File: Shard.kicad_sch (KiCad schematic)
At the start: 5 parts, among them J1 USB_C_Receptacle_USB2.0_16P, U1 ESP32-S3

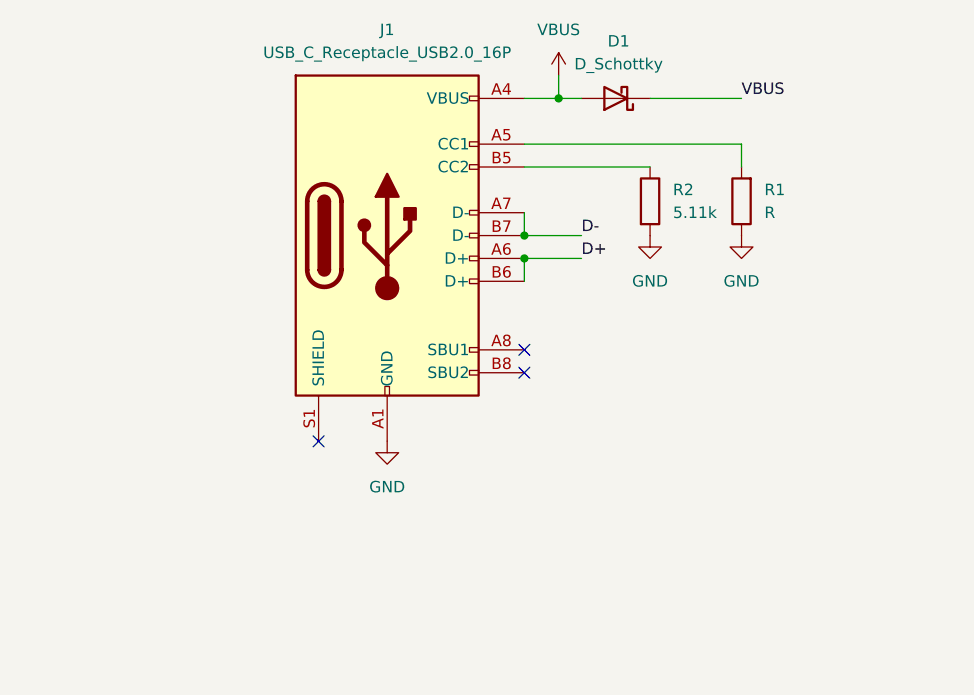
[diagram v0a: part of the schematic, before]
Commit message: USB-C Wiring
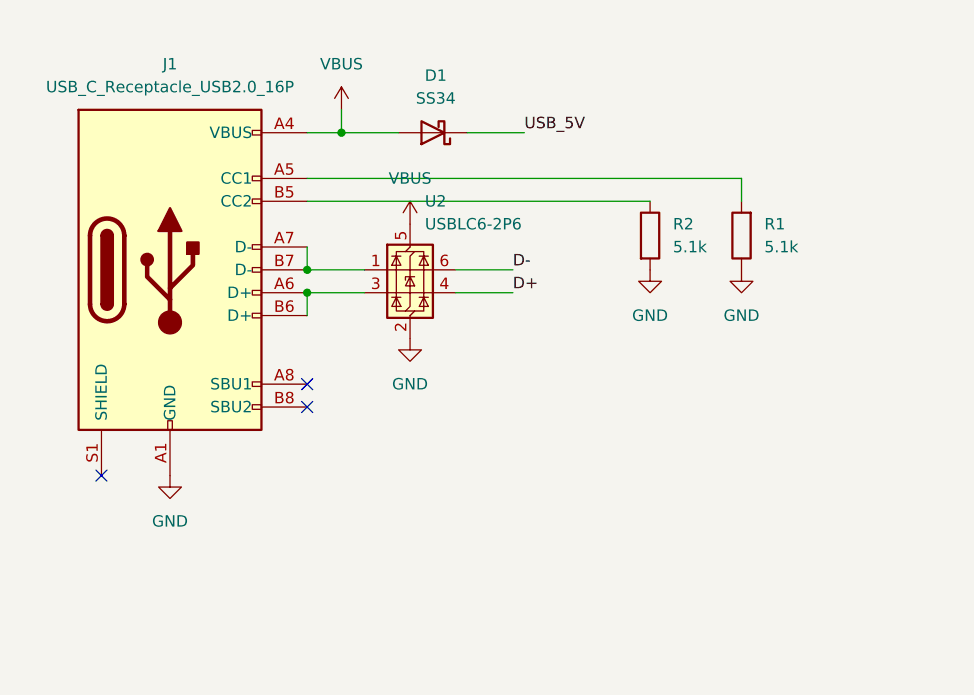
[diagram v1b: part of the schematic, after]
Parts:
- added U2: USBLC6-2P6, Package_TO_SOT_SMD:SOT-666, symbol Power_Protection:USBLC6-2P6
- D1: value D_Schottky -> SS34; footprint (none) -> Diode_SMD:D_SMA; REF (none) -> C8678
- J1: footprint (none) -> Connector_USB:USB_C_Receptacle_GCT_USB4105-xx-A_16P_TopMnt_Horizontal; REF (none) -> C2927038
- R1: value R -> 5.1k; footprint (none) -> Resistor_SMD:R_0402_1005Metric; REF (none) -> C294638
- R2: value 5.11k -> 5.1k; footprint (none) -> Resistor_SMD:R_0402_1005Metric; REF (none) -> C294638
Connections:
- net D+: now also U2.4 (I/O2); no longer J1.A6 (D+), J1.B6 (D+)
- net D-: now also U2.6 (I/O1); no longer J1.A7 (D-), J1.B7 (D-)
- net GND: now also U2.2 (GND)
- net VBUS: now also U2.5 (VBUS); no longer D1.1 (K)
- new net: J1.A6 (D+), J1.B6 (D+), U2.3 (I/O2)
- new net: J1.A7 (D-), J1.B7 (D-), U2.1 (I/O1)
- new net USB_5V: D1.1 (K)
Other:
- moved on the sheet: D1, J1, R1, R2

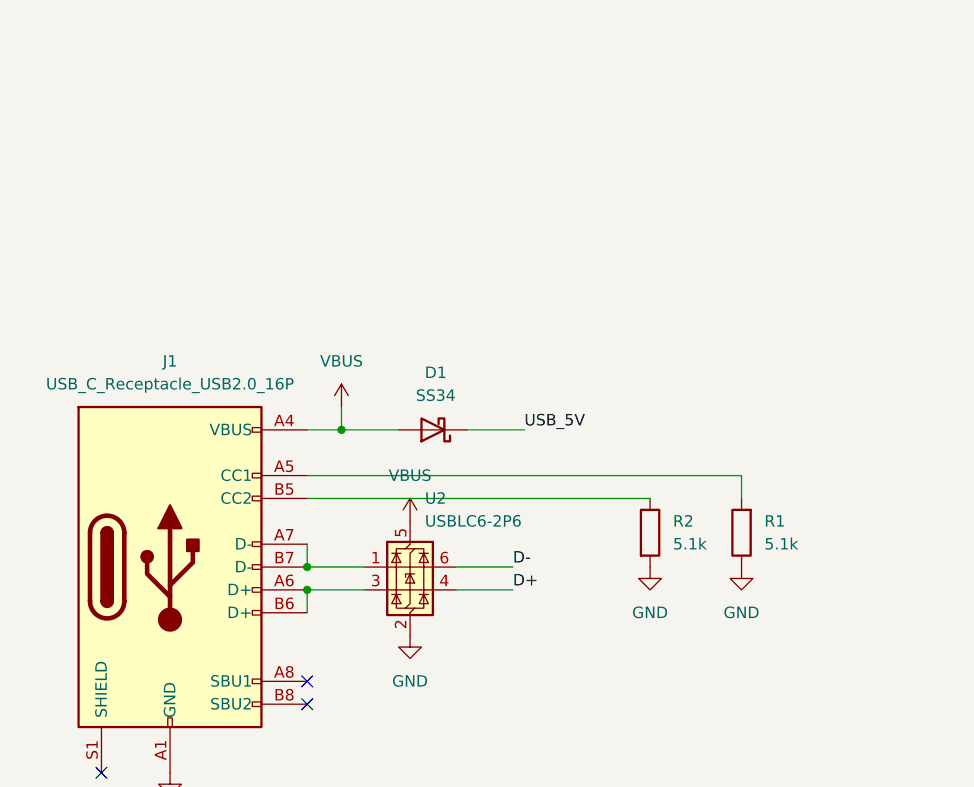
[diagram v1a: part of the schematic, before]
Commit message: Add voltage regulator
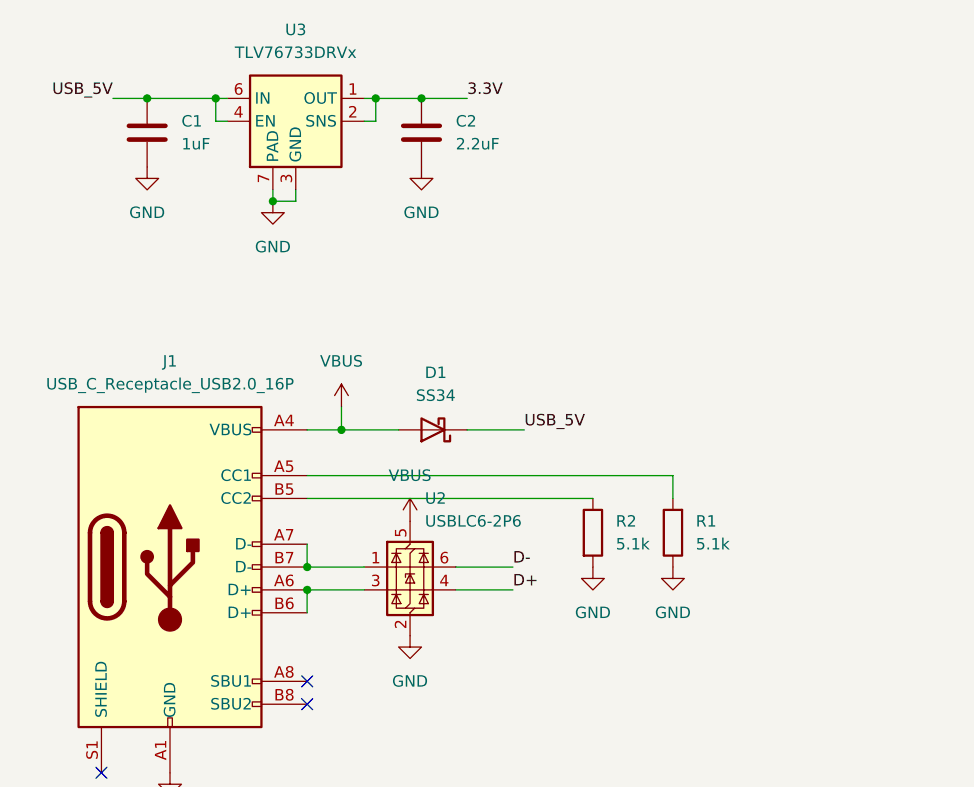
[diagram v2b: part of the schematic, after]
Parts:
- added C1: 1uF, Capacitor_SMD:C_0603_1608Metric, symbol Device:C
- added C2: 2.2uF, Capacitor_SMD:C_0402_1005Metric, symbol Device:C
- added U3: TLV76733DRVx, Package_SON:WSON-6-1EP_2x2mm_P0.65mm_EP1x1.6mm_ThermalVias, symbol Regulator_Linear:TLV76733DRVx
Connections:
- net GND: now also C1.2, C2.2, U3.3 (GND), U3.5 (GND), U3.7 (PAD)
- net USB_5V: now also C1.1, U3.4 (EN), U3.6 (IN)
- new net 3.3V: C2.1, U3.1 (OUT), U3.2 (SNS)
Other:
- moved on the sheet: R1, R2

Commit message: Add battery connector
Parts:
- added D2: SS34, Diode_SMD:D_SMA, symbol Device:D_Schottky
- added J2: Conn_01x02_Pin, symbol Connector:Conn_01x02_Pin
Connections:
- net GND: now also J2.2 (Pin_2)
- net USB_5V renamed V_BAT
- net V_BAT: now also D2.1 (K)
- new net: D2.2 (A), J2.1 (Pin_1)

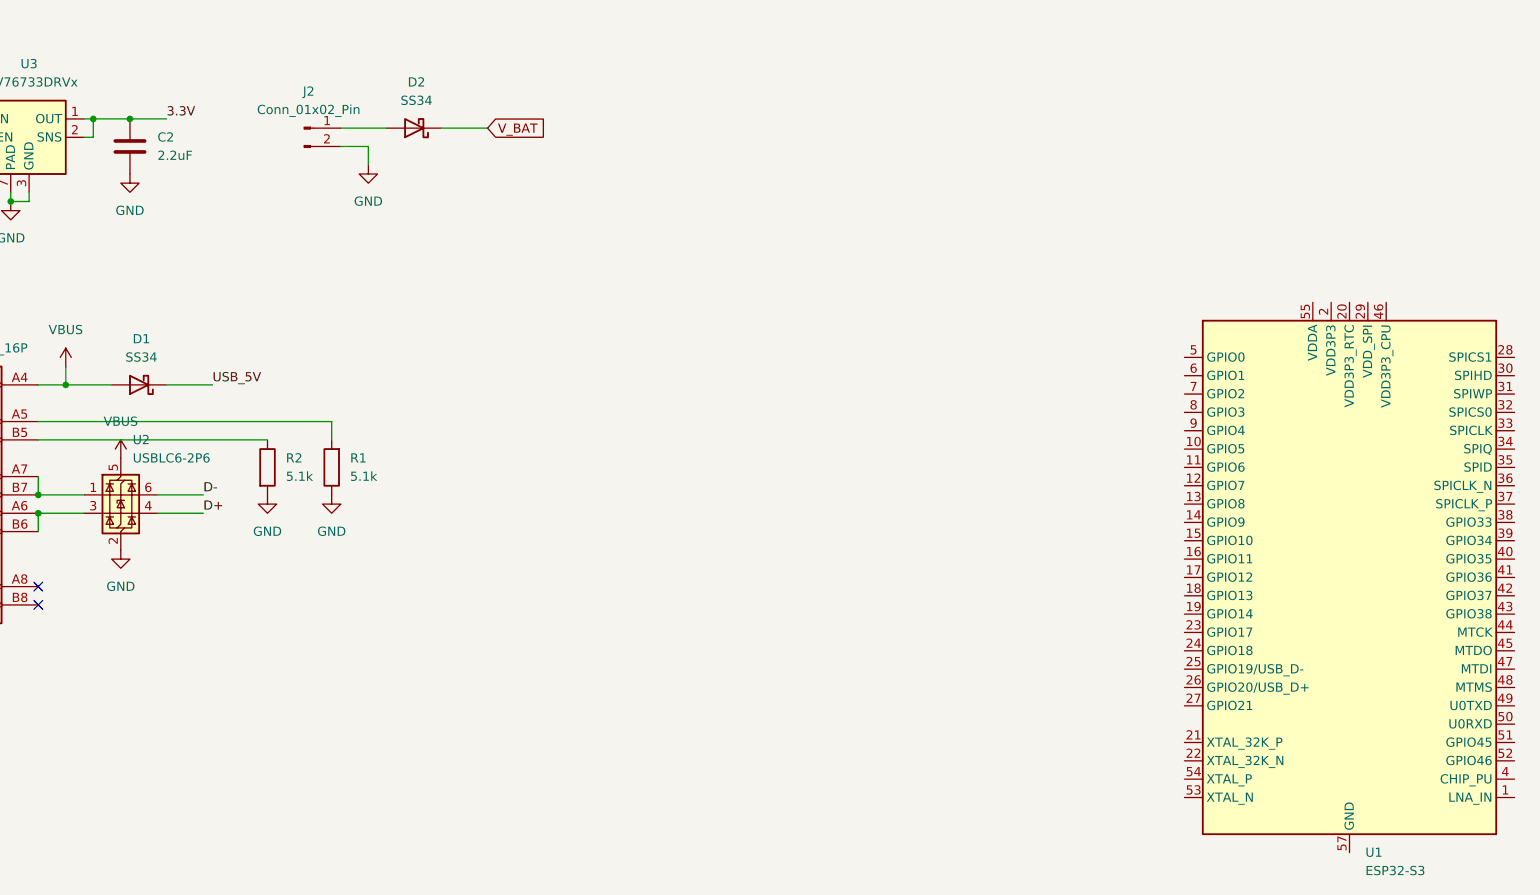
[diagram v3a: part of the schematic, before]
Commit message: Add missing footprint and parts
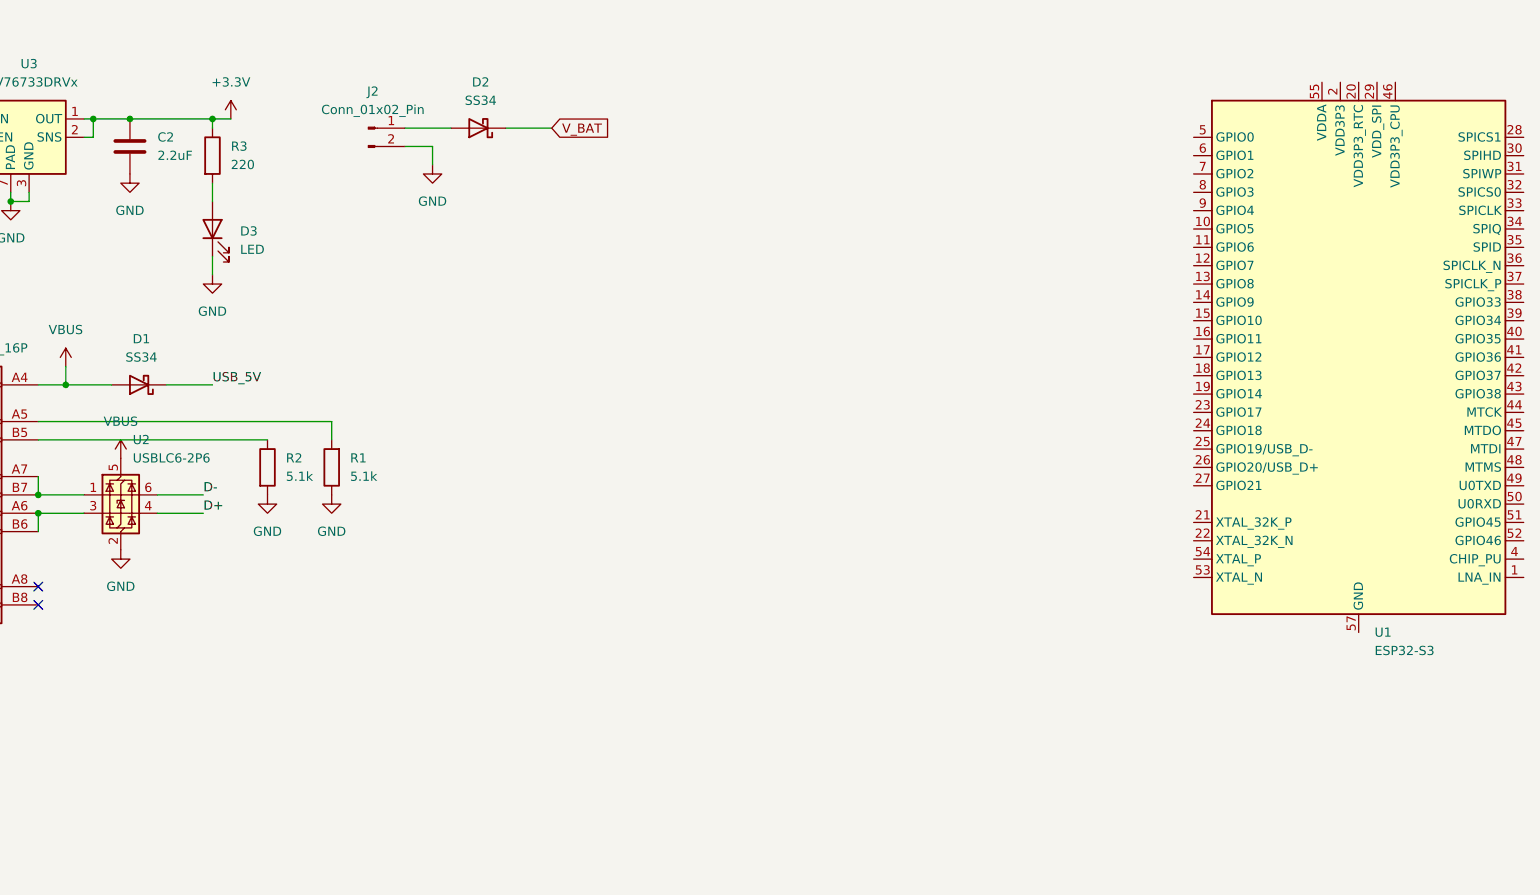
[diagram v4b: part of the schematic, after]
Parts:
- added D3: LED, LED_SMD:LED_0805_2012Metric, symbol Device:LED
- added R3: 220, Resistor_SMD:R_0805_2012Metric, symbol Device:R
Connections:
- net GND: now also D3.1 (K)
- net 3.3V renamed +3.3V
- net +3.3V: now also R3.1
- new net: D3.2 (A), R3.2
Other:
- moved on the sheet: D2, J2, U1

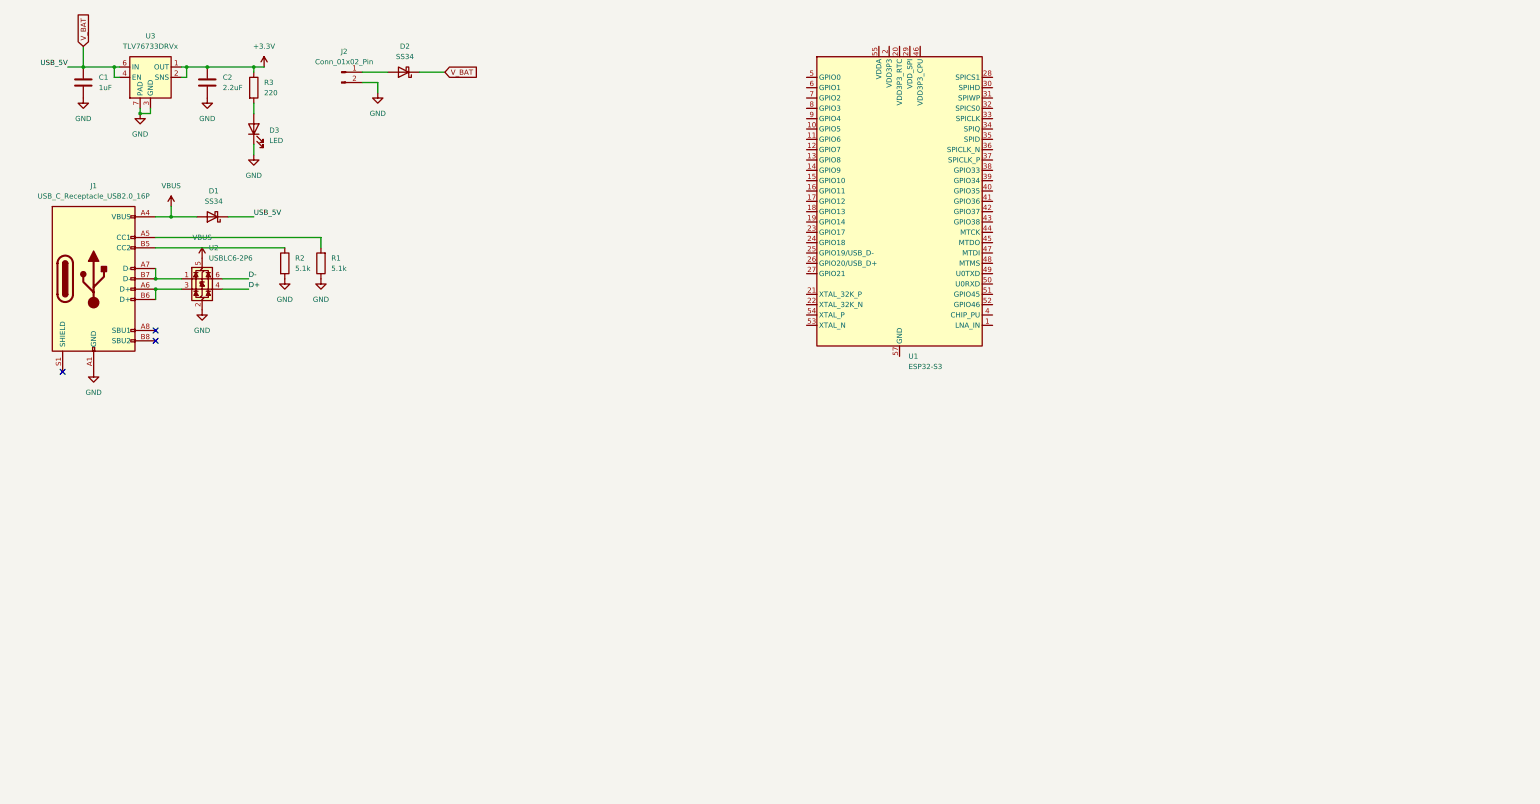
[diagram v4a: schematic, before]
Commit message: Add MCU power schematic + Footprint and part assignation
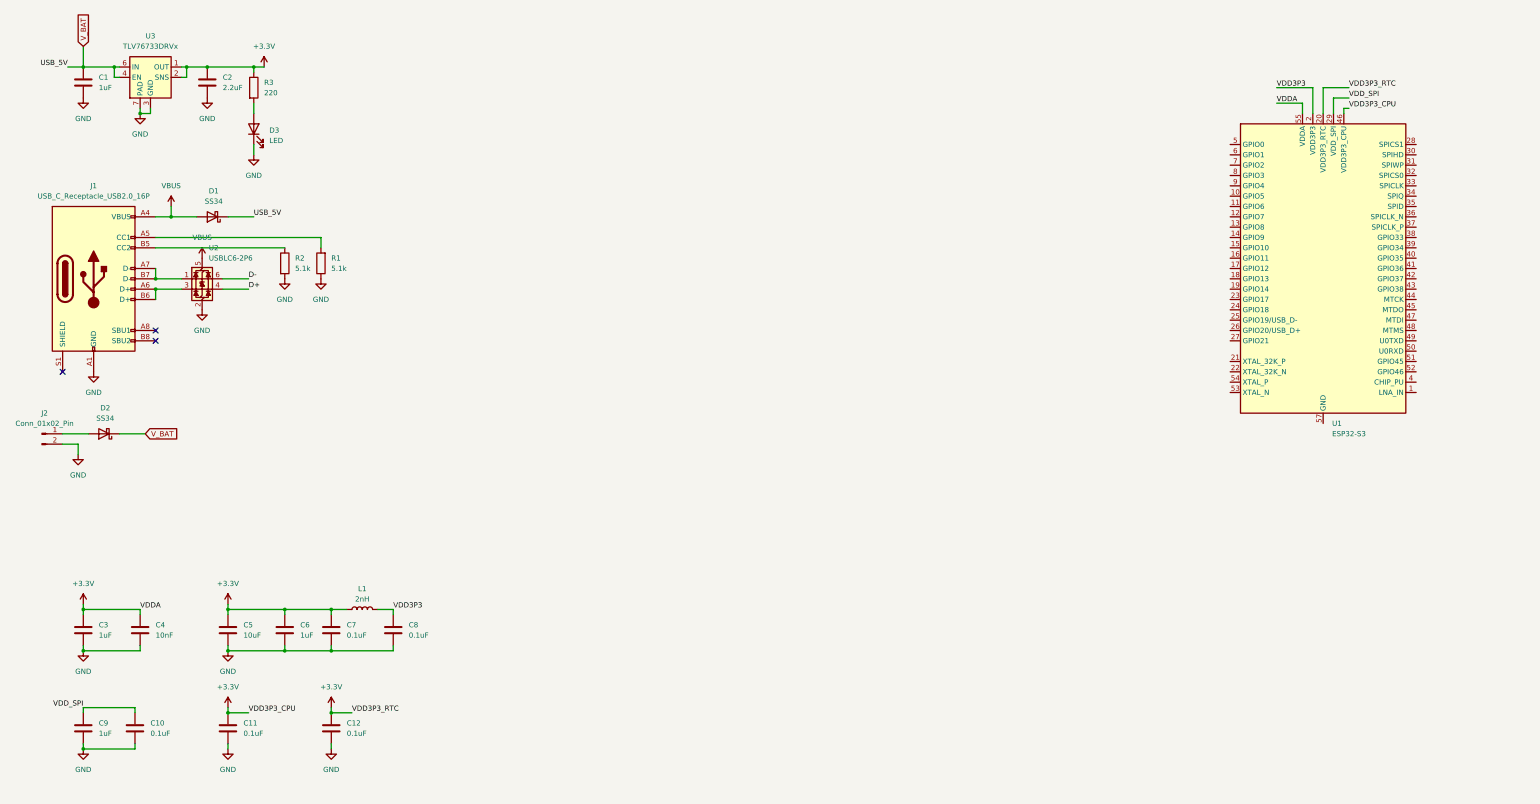
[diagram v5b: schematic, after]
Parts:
- added C10, C11, C12, C7, C8: 0.1uF, Capacitor_SMD:C_1206_3216Metric, symbol Device:C
- added C3, C6, C9: 1uF, Capacitor_SMD:C_0603_1608Metric, symbol Device:C
- added C4: 10nF, Capacitor_SMD:C_1206_3216Metric, symbol Device:C
- added C5: 10uF, Capacitor_SMD:C_0805_2012Metric, symbol Device:C
- added L1: 2nH, symbol Device:L
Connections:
- net +3.3V: now also U1.20 (VDD3P3_RTC), U1.46 (VDD3P3_CPU), U1.55 (VDDA), U1.56 (VDDA), C11.1, C12.1, C3.1, C4.1, C5.1, C6.1, C7.1, L1.1
- net GND: now also C10.2, C11.2, C12.2, C3.2, C4.2, C5.2, C6.2, C7.2, C8.2, C9.2
- net VDD3P3: now reaches U1.2 (VDD3P3), U1.3 (VDD3P3)
- net VDD3P3: now also C8.1, L1.2
- net VDD_SPI: now reaches U1.29 (VDD_SPI)
- net VDD_SPI: now also C10.1, C9.1
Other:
- moved on the sheet: D2, J2, U1

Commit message: Add missing inductor footprint + LDO for external 3.3V alimentation.
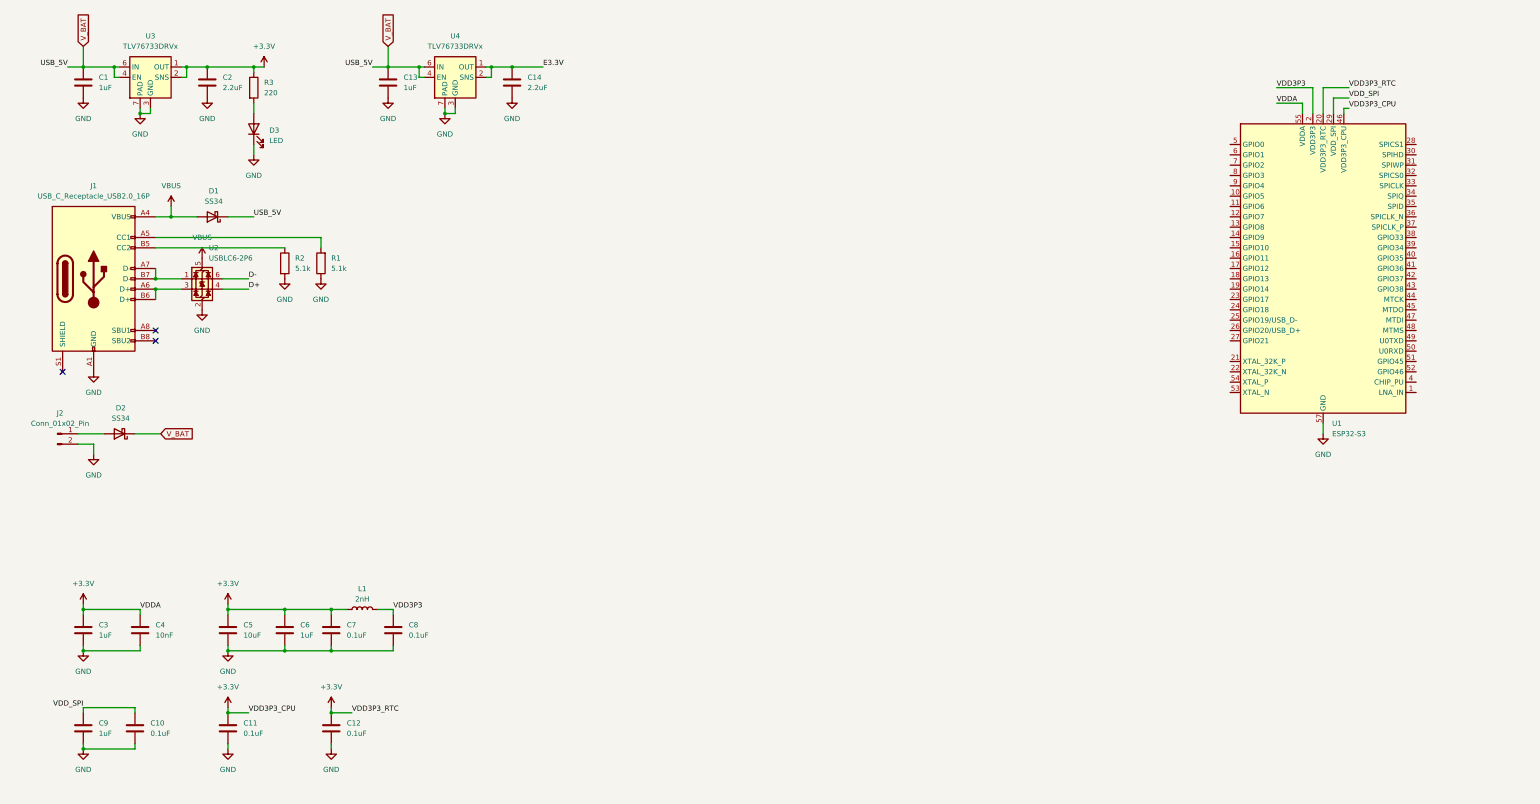
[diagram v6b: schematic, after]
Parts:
- added C13: 1uF, Capacitor_SMD:C_0603_1608Metric, symbol Device:C
- added C14: 2.2uF, Capacitor_SMD:C_0402_1005Metric, symbol Device:C
- added U4: TLV76733DRVx, Package_SON:WSON-6-1EP_2x2mm_P0.65mm_EP1x1.6mm_ThermalVias, symbol Regulator_Linear:TLV76733DRVx
- L1: footprint (none) -> Inductor_SMD:L_0201_0603Metric; REF (none) -> C415347
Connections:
- net GND: now also U1.57 (GND), C13.2, C14.2, U4.3 (GND), U4.5 (GND), U4.7 (PAD)
- net V_BAT: now also C13.1, U4.4 (EN), U4.6 (IN)
- new net E3.3V: C14.1, U4.1 (OUT), U4.2 (SNS)
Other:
- moved on the sheet: D2, J2
